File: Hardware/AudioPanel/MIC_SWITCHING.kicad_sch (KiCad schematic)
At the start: 22 parts, among them U119 ADG729, U120 ADG729, U122 MCP6004, U123 ADS7830, U124 MCP6004, U125 MCP47FVB08, U126 MCP47FVB08

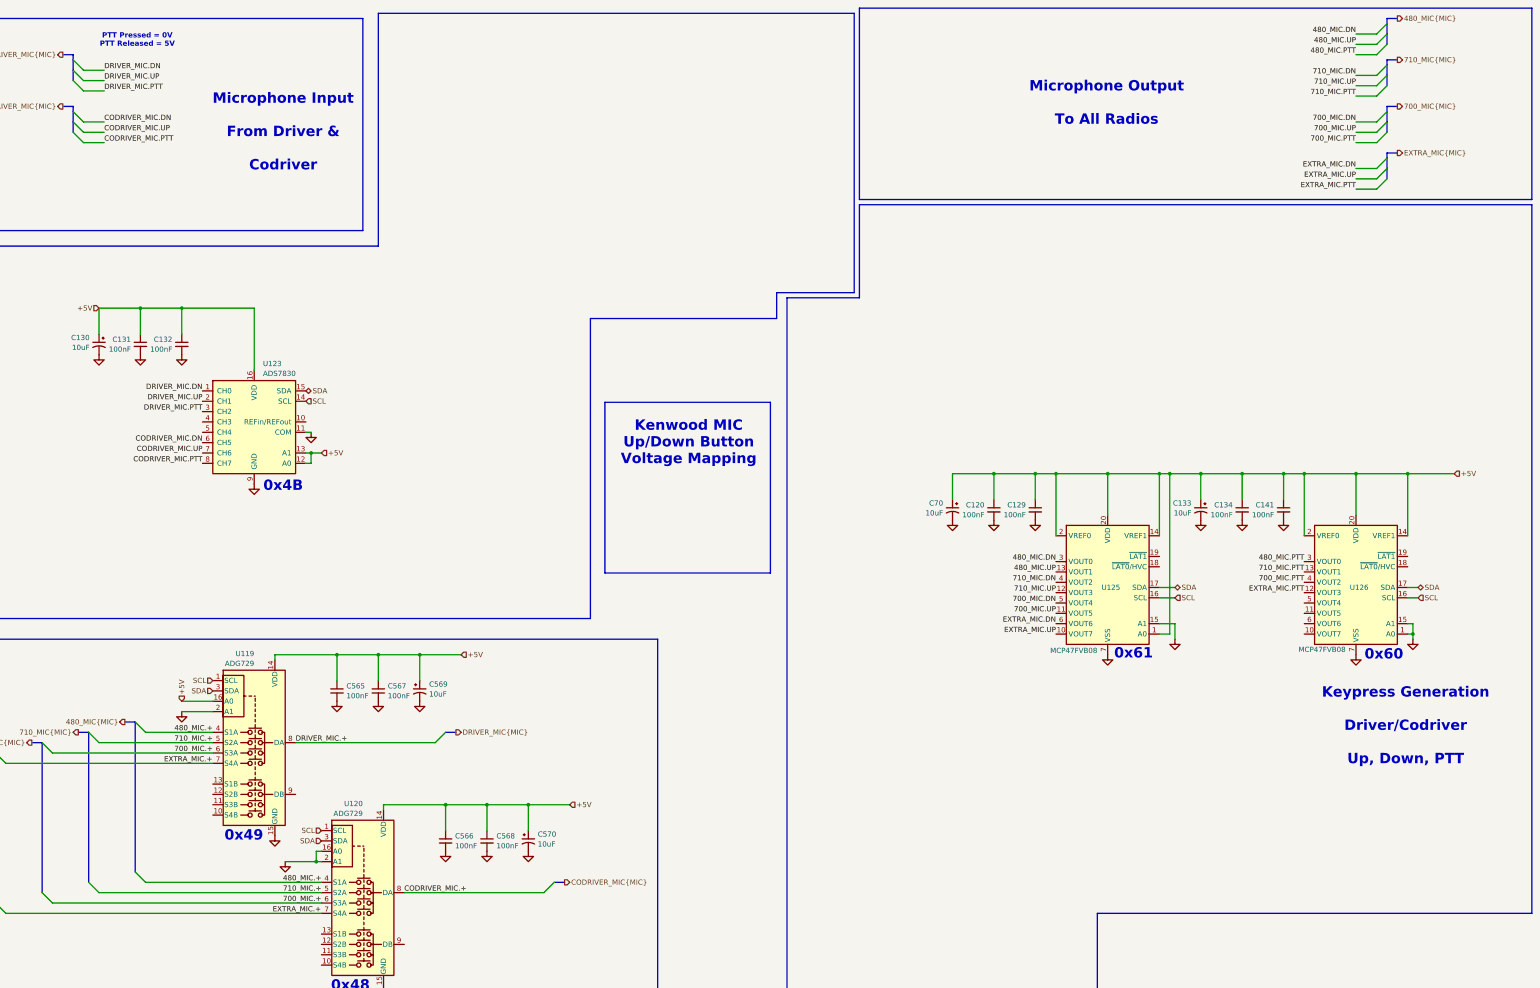
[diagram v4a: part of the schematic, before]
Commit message: Realized that I need to rethink how I'm going to mix the radio audio with the stereo audio
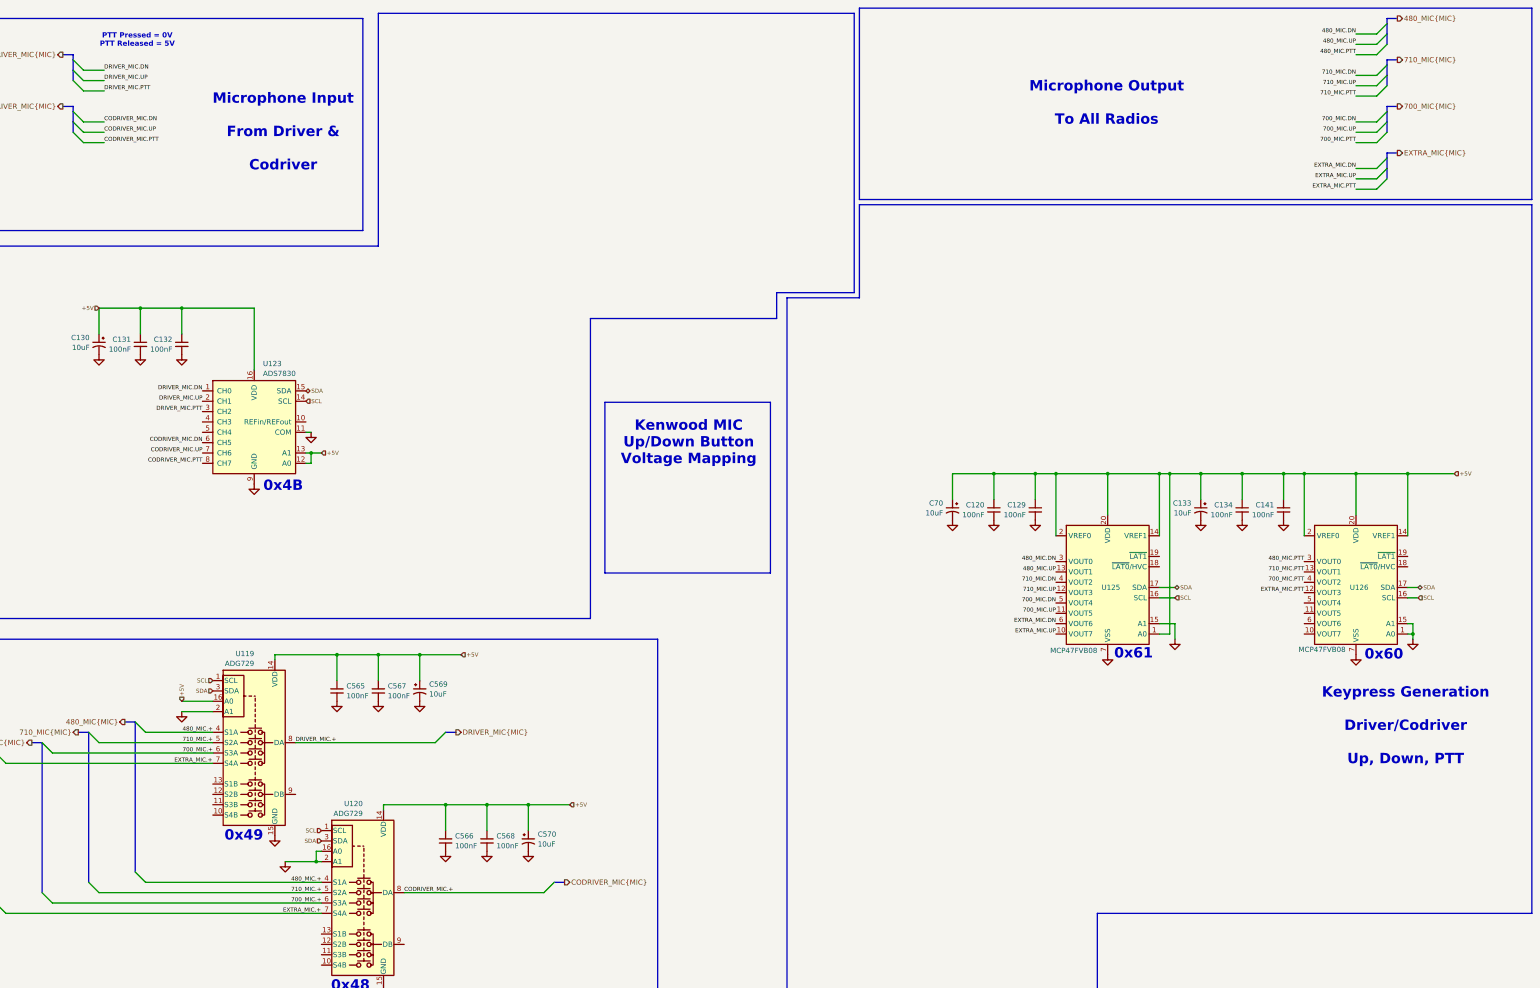
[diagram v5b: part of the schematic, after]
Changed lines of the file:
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@@
 	)
 	(bus_alias "UP_TO_RADIO"
-		(members "UP" "DOWN" "PTT" "+")
+		(members "FL" "FR" "RL" "RR" "SL" "SR")
 	)
 	(rectangle
@@
 			"AEkAeQBPAGoAcwBiAEgAeABSAHcAMABBAEUAeABVAFYAQgBiAGsATgBsAHkANQBkACsAcQBQAEgA"
 			"MABsADMATwBuAHoAOABQADMANgBtADcAdQB6AHUANQBmAE8ALwBlAHYAWABqADIAMgB0AHYAYgBr"
-			"ADkAKwA2AGQAZQBzAFcAYQBHAGsANwBPAHoAdQ=="
+			"ADkAKwA2AGQAZQBzAFcAYQBHAGsANwBPAHoAdQBQADcAZwAvAGoAZQAzAFAAZwB3AEEARQBZAEYA"
+			"WQAvAEgARQAxAGgAaAB5ADUAWQB0AFEAagA3AEwAcwBtAFgATABjAE0AMgAxAGEAOQBkACsAOABy"
+			"AE4AMwBkAEgAVAB3AFgANgBLADAAdABCAFEAaABwAEsAdQByAG0ANQBtAFoAKwBiADAAKwBKAHcA"
+			"MABOAEQAUQAwAE4ARABRADMATgBQADQAQgB1AEsAVwBRAGUAagB3AGYARwBsAGoAWQAyAE4AbgBC"
+			"AFEARQB4AFUAVgBoAFQAMABiADgAWQBxADIAbwBxAEoAQwBWAEYAUQBVAEkAUwBRAHIASwAwAHMA"
+			"UQBCAEYAawBoAFIAMABWAEYAWQBVAFcATgBFAEwASwAxAHQAWQAyAE4AagBTAFUAcgBaAEgARgB4"
+			"AGMAUgBjAFgARgB4AGMAWABGADIATgBqAFkAeQBnADUAZQBQAEMAZwB3AE0ARQBJAFYAOABnAEMA"
+			"RQBSAE0AVABtAHoAeAA1AGMAbgAxADkAUABSADYAbgBqAFkAMABOAHYAegB2AGwAVAB6AC8AOQA5"
+			"AFAASABqAFIAeQBIADMAUQBVAEoAQwB3AHQARABRAE0ARABJAHkAVQBsAHAAYQBtAHMARgBnAGkA"
+			"SQB1AEwAeAA4AGYASABYADcAaAB3AFEAVgB4AGMAbgBNAEYAZwBpAEkAbQBKAGkAWQB1AEwANwA5"
+			"AHEAMQA2ADkAMgA3AGQAdwBSAEIAcABLAGUAbgBpADQAdQBMAGkANAB1AEwAQgB3AGMASABRAC8A"
+			"TwBHAGgAbwBiAEoAawB5AGQARABJAFgAeABrAEQAdwArAFAASgAwACsAZQB3AEwAdQB2AFgAcgAw"
+			"AHkATQBqAEwANgAvAGYAZgBmADMANwB4ADUAMAA3AGQAdgBYADMARgB4AGMAVABnAFAASgB3AGcA"
+			"aQBPAGoAcAA2ADgATwBEAEIANABwADEATQBtAGoAUwBKAGYASQBpAFgAbABwAFkAbQBLAFMAawBa"
+			"AEYAQgBUADAAKwBQAEYAagBkADMAZAAzAHEARwBOAHAAYQBSAGsAVABFADAATQBlAFAAQwBqAGsA"
+			"TQBXAFAARwBSAEUAWgBHAGoAaABzADMAVABsAHgAYwBYAEYAOQBmAFAAegBJAHkAcwBxADIAdABq"
+			"AFYAdwB0AEsAeQBzAHIATQBqAEoAeQArAFAARABoADQAdQBMAGkASgBpAFkAbQBrAFoARwBSAFoA"
+			"QwBWAFQAVwAxAHMAYgBHAFIAawBaAEcAUgBsAFoAVQBsAEsAUwBtAFoAbQBwAHEAcQBvAHEATABp"
+			"ADQAKwBaAGMAcQBVAHgATQBSAEUALwB0AHYAMQ=="
 		)
 	)
@@
 		(effects
 			(font
-				(size 1.27 1.27)
+				(size 1 1)
 			)
 			(justify right bottom)
@@
 		(effects
 			(font
-				(size 1.27 1.27)
+				(size 1 1)
 			)
 			(justify right bottom)
@@
 		(effects
 			(font
-				(size 1.27 1.27)
+				(size 1 1)
 			)
 			(justify right bottom)
@@
 		(effects
 			(font
-				(size 1.27 1.27)
+				(size 1 1)
 			)
 			(justify right bottom)
@@
 		(effects
 			(font
-				(size 1.27 1.27)
+				(size 1 1)
 			)
 			(justify left bottom)
@@
 		(effects
 			(font
-				(size 1.27 1.27)
+				(size 1 1)
 			)
 			(justify right bottom)
@@
 		(effects
 			(font
-				(size 1.27 1.27)
+				(size 1 1)
 			)
 			(justify right bottom)
@@
 		(effects
 			(font
-				(size 1.27 1.27)
+				(size 1 1)
 			)
 			(justify right bottom)
@@
 		(effects
 			(font
-				(size 1.27 1.27)
+				(size 1 1)
 			)
 			(justify right bottom)
@@
 		(effects
 			(font
-				(size 1.27 1.27)
+				(size 1 1)
 			)
 			(justify right bottom)
@@
 		(effects
 			(font
-				(size 1.27 1.27)
+				(size 1 1)
 			)
 			(justify left bottom)
@@
 		(effects
 			(font
-				(size 1.27 1.27)
+				(size 1 1)
 			)
 			(justify left bottom)
@@
 		(effects
 			(font
-				(size 1.27 1.27)
+				(size 1 1)
 			)
 			(justify right bottom)
@@
 		(effects
 			(font
-				(size 1.27 1.27)
+				(size 1 1)
 			)
 			(justify right bottom)
@@
 		(effects
 			(font
-				(size 1.27 1.27)
+				(size 1 1)
 			)
 			(justify right bottom)
@@
 		(effects
 			(font
-				(size 1.27 1.27)
+				(size 1 1)
 			)
 			(justify right bottom)
@@
 		(effects
 			(font
-				(size 1.27 1.27)
+				(size 1 1)
 			)
 			(justify right bottom)
@@
 		(effects
 			(font
-				(size 1.27 1.27)
+				(size 1 1)
 			)
 			(justify right bottom)
@@
 		(effects
 			(font
-				(size 1.27 1.27)
+				(size 1 1)
 			)
 			(justify right bottom)
@@
 		(effects
 			(font
-				(size 1.27 1.27)
+				(size 1 1)
 			)
 			(justify left bottom)
@@
 		(effects
 			(font
-				(size 1.27 1.27)
+				(size 1 1)
 			)
 			(justify right bottom)
@@
 		(effects
 			(font
-				(size 1.27 1.27)
+				(size 1 1)
 			)
 			(justify right bottom)
@@
 		(effects
 			(font
-				(size 1.27 1.27)
+				(size 1 1)
 			)
 			(justify right bottom)
@@
 		(effects
 			(font
-				(size 1.27 1.27)
+				(size 1 1)
 			)
 			(justify right bottom)
@@
 		(effects
 			(font
-				(size 1.27 1.27)
+				(size 1 1)
 			)
 			(justify right bottom)
@@
 		(effects
 			(font
-				(size 1.27 1.27)
+				(size 1 1)
 			)
 			(justify right bottom)
@@
 		(effects
 			(font
-				(size 1.27 1.27)
+				(size 1 1)
 			)
 			(justify right bottom)
@@
 		(effects
 			(font
-				(size 1.27 1.27)
+				(size 1 1)
 			)
 			(justify right bottom)
@@
 		(effects
 			(font
-				(size 1.27 1.27)
+				(size 1 1)
 			)
 			(justify right bottom)
@@
 		(effects
 			(font
-				(size 1.27 1.27)
+				(size 1 1)
 			)
 			(justify left bottom)
@@
 		(effects
 			(font
-				(size 1.27 1.27)
+				(size 1 1)
 			)
 			(justify right bottom)
@@
 		(effects
 			(font
-				(size 1.27 1.27)
+				(size 1 1)
 			)
 			(justify right bottom)
@@
 		(effects
 			(font
-				(size 1.27 1.27)
+				(size 1 1)
 			)
 			(justify right bottom)
@@
 		(effects
 			(font
-				(size 1.27 1.27)
+				(size 1 1)
 			)
 			(justify right bottom)
@@
 		(effects
 			(font
-				(size 1.27 1.27)
+				(size 1 1)
 			)
 			(justify left bottom)
@@
 		(effects
 			(font
-				(size 1.27 1.27)
+				(size 1 1)
 			)
 			(justify right bottom)
@@
 		(effects
 			(font
-				(size 1.27 1.27)
+				(size 1 1)
 			)
 			(justify left bottom)
@@
 		(effects
 			(font
-				(size 1.27 1.27)
+				(size 1 1)
 			)
 			(justify right bottom)
@@
 		(effects
 			(font
-				(size 1.27 1.27)
+				(size 1 1)
 			)
 			(justify right bottom)
@@
 		(effects
 			(font
-				(size 1.27 1.27)
+				(size 1 1)
 			)
 			(justify right bottom)
@@
 		(effects
 			(font
-				(size 1.27 1.27)
+				(size 1 1)
 			)
 			(justify right bottom)
@@
 		(effects
 			(font
-				(size 1.27 1.27)
+				(size 1 1)
 			)
 			(justify right bottom)
@@
 		(effects
 			(font
-				(size 1.27 1.27)
+				(size 1 1)
 			)
 			(justify right bottom)
@@
 		(effects
 			(font
-				(size 1.27 1.27)
+				(size 1 1)
 			)
 			(justify right bottom)
@@
 		(effects
 			(font
-				(size 1.27 1.27)
+				(size 1 1)
 			)
 			(justify left bottom)
@@
 		(effects
 			(font
-				(size 1.27 1.27)
+				(size 1 1)
 			)
 			(justify right bottom)
@@
 		(effects
 			(font
-				(size 1.27 1.27)
+				(size 1 1)
 			)
 			(justify left)
@@
 		(effects
 			(font
-				(size 1.27 1.27)
+				(size 1 1)
 			)
 			(justify left)
@@
 		(effects
 			(font
-				(size 1.27 1.27)
+				(size 1 1)
 			)
 			(justify right)
@@
 		(effects
 			(font
-				(size 1.27 1.27)
+				(size 1 1)
 			)
 			(justify right)
@@
 		(effects
 			(font
-				(size 1.27 1.27)
+				(size 1 1)
 			)
 			(justify left)
@@
 		(effects
 			(font
-				(size 1.27 1.27)
+				(size 1 1)
 			)
 			(justify left)
@@
 		(effects
 			(font
-				(size 1.27 1.27)
+				(size 1 1)
 			)
 			(justify right)
@@
 		(effects
 			(font
-				(size 1.27 1.27)
+				(size 1 1)
 			)
 			(justify left)
@@
 		(effects
 			(font
-				(size 1.27 1.27)
+				(size 1 1)
 			)
 			(justify left)
@@
 		(effects
 			(font
-				(size 1.27 1.27)
+				(size 1 1)
 			)
 			(justify right)
@@
 		(effects
 			(font
-				(size 1.27 1.27)
+				(size 1 1)
 			)
 			(justify left)
@@
 		(effects
 			(font
-				(size 1.27 1.27)
+				(size 1 1)
 			)
 			(justify left)
@@
 		(effects
 			(font
-				(size 1.27 1.27)
+				(size 1 1)
 			)
 			(justify left)
@@
 		(effects
 			(font
-				(size 1.27 1.27)
+				(size 1 1)
 			)
 			(justify right)
@@
 		(effects
 			(font
-				(size 1.27 1.27)
+				(size 1 1)
 			)
 			(justify left)
@@
 		(effects
 			(font
-				(size 1.27 1.27)
+				(size 1 1)
 			)
 			(justify left)

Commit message: Cleaned up stuff, defined more busses
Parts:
- removed C565, C566, C567, C568: 100nF, symbol Device:C_Small
- removed C569, C570: 10uF, symbol Device:C_Polarized_Small_US
- removed U119, U120: ADG729, Package_SO:TSSOP-16_4.4x5mm_P0.65mm, symbol Analog_Switch:ADG729
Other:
- added sheet 4x4 Crosspoint Switch (Crosspoint_4x4_4066.kicad_sch)
- note removed: "0x48"
- note removed: "0x49"
